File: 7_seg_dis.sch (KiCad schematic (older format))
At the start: 30 parts, among them U10 HDSP-7401, U5 74HC595, U6 74HC595, U7 74HC595, U8 HDSP-7401, U9 HDSP-7401

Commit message: reorganized schematic; added reverse polarity protection; start adding footprints
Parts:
- removed U10, U8, U9: HDSP-7401, Display_7Segment:HDSP-7401, symbol Display_Character:HDSP-7401
- added U? (x3): HDSP-7403, Display_7Segment:HDSP-7401, symbol Display_Character:HDSP-7403
- R10, R11, R12, R13, R14, R15, R16, R17, R18, R19, R20, R21, R22, R23, R24, R25, R26, R27, R4, R5, R6, R7, R8, R9: value R -> 330
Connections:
- net labels added: CLK, QH', RCLK, SER
- net labels removed: 7seg_POWER, SPI_1_CLK, SPI_1_CS, SPI_1_MOSI
- wire segments 174 -> 207
- no-connect marks 1 -> 0
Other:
- moved on the sheet: R10, R11, R12, R13, R14, R15, R16, R17, R18, R19, R20, R21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

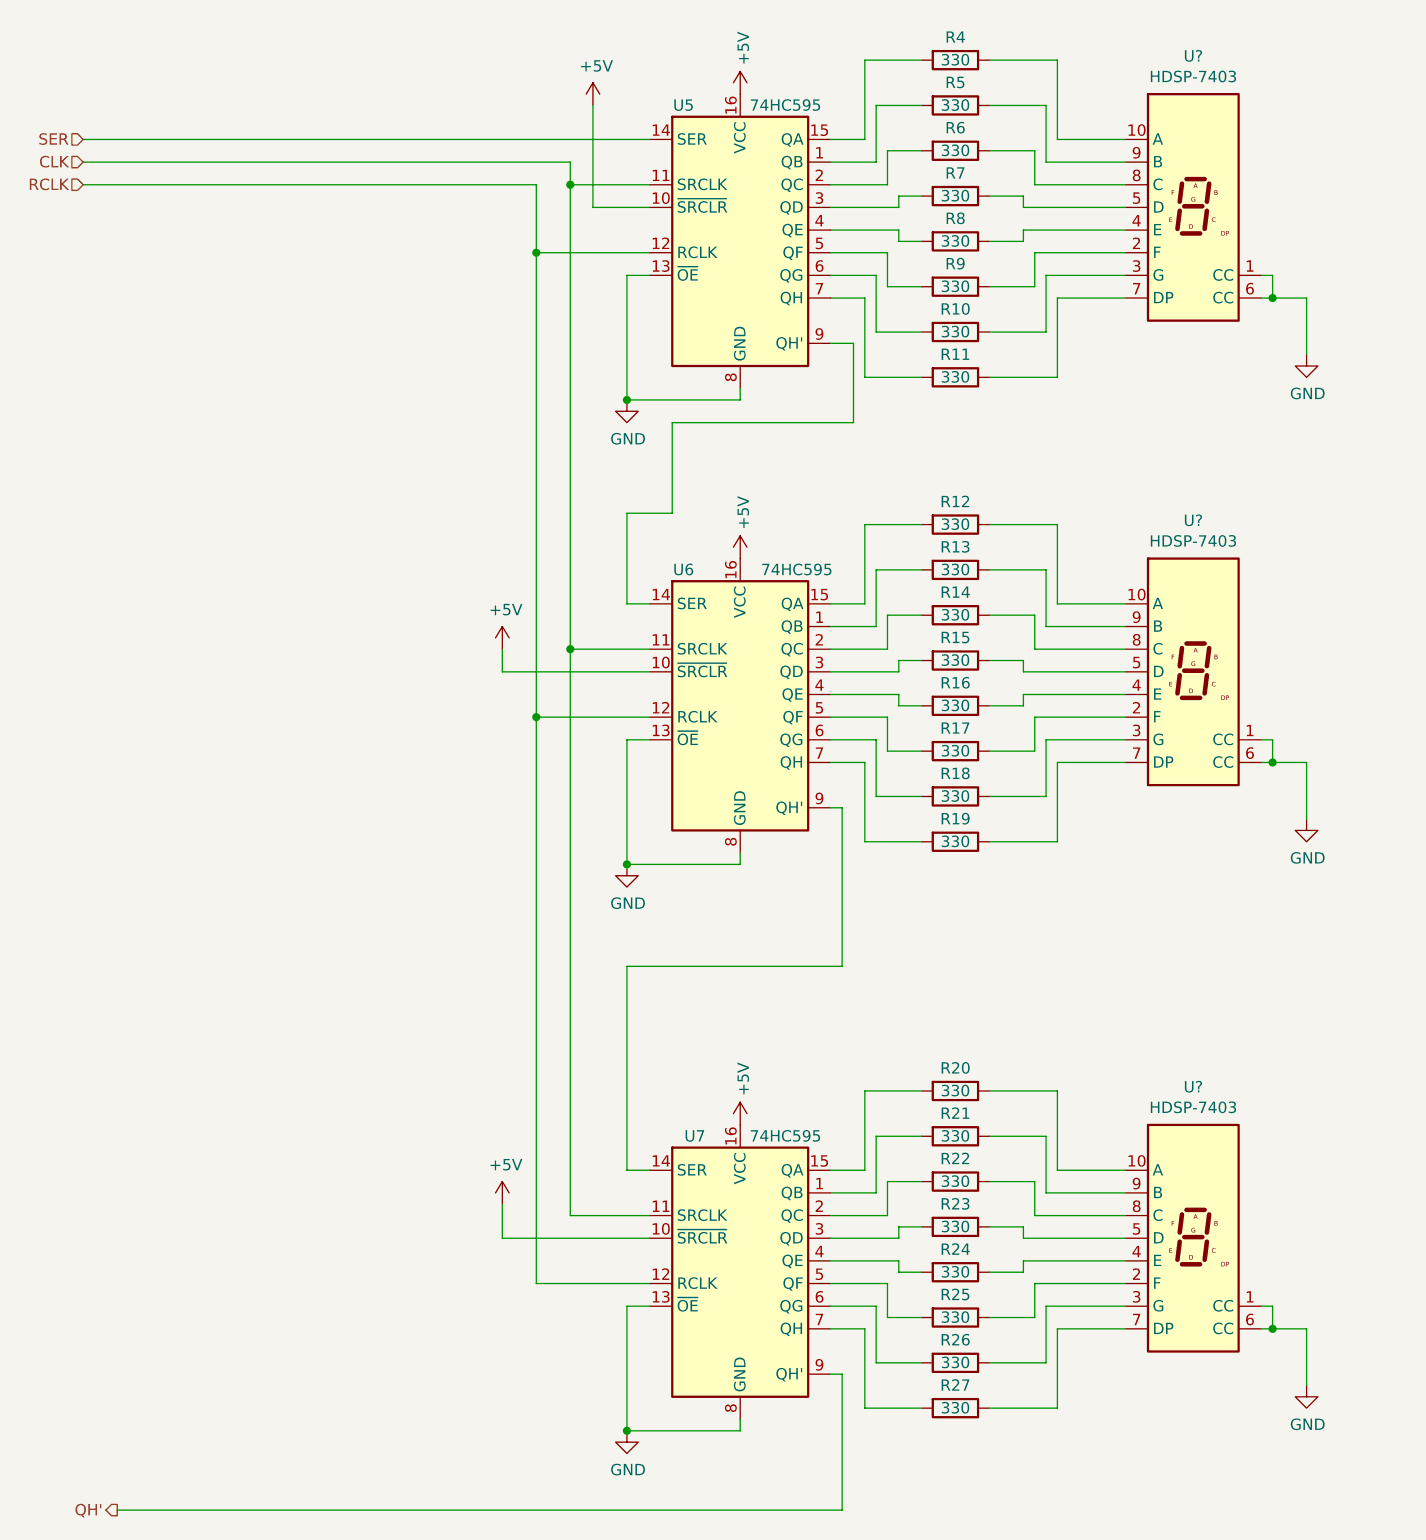
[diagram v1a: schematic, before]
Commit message: footprints; library for 7seg; start pcb layout
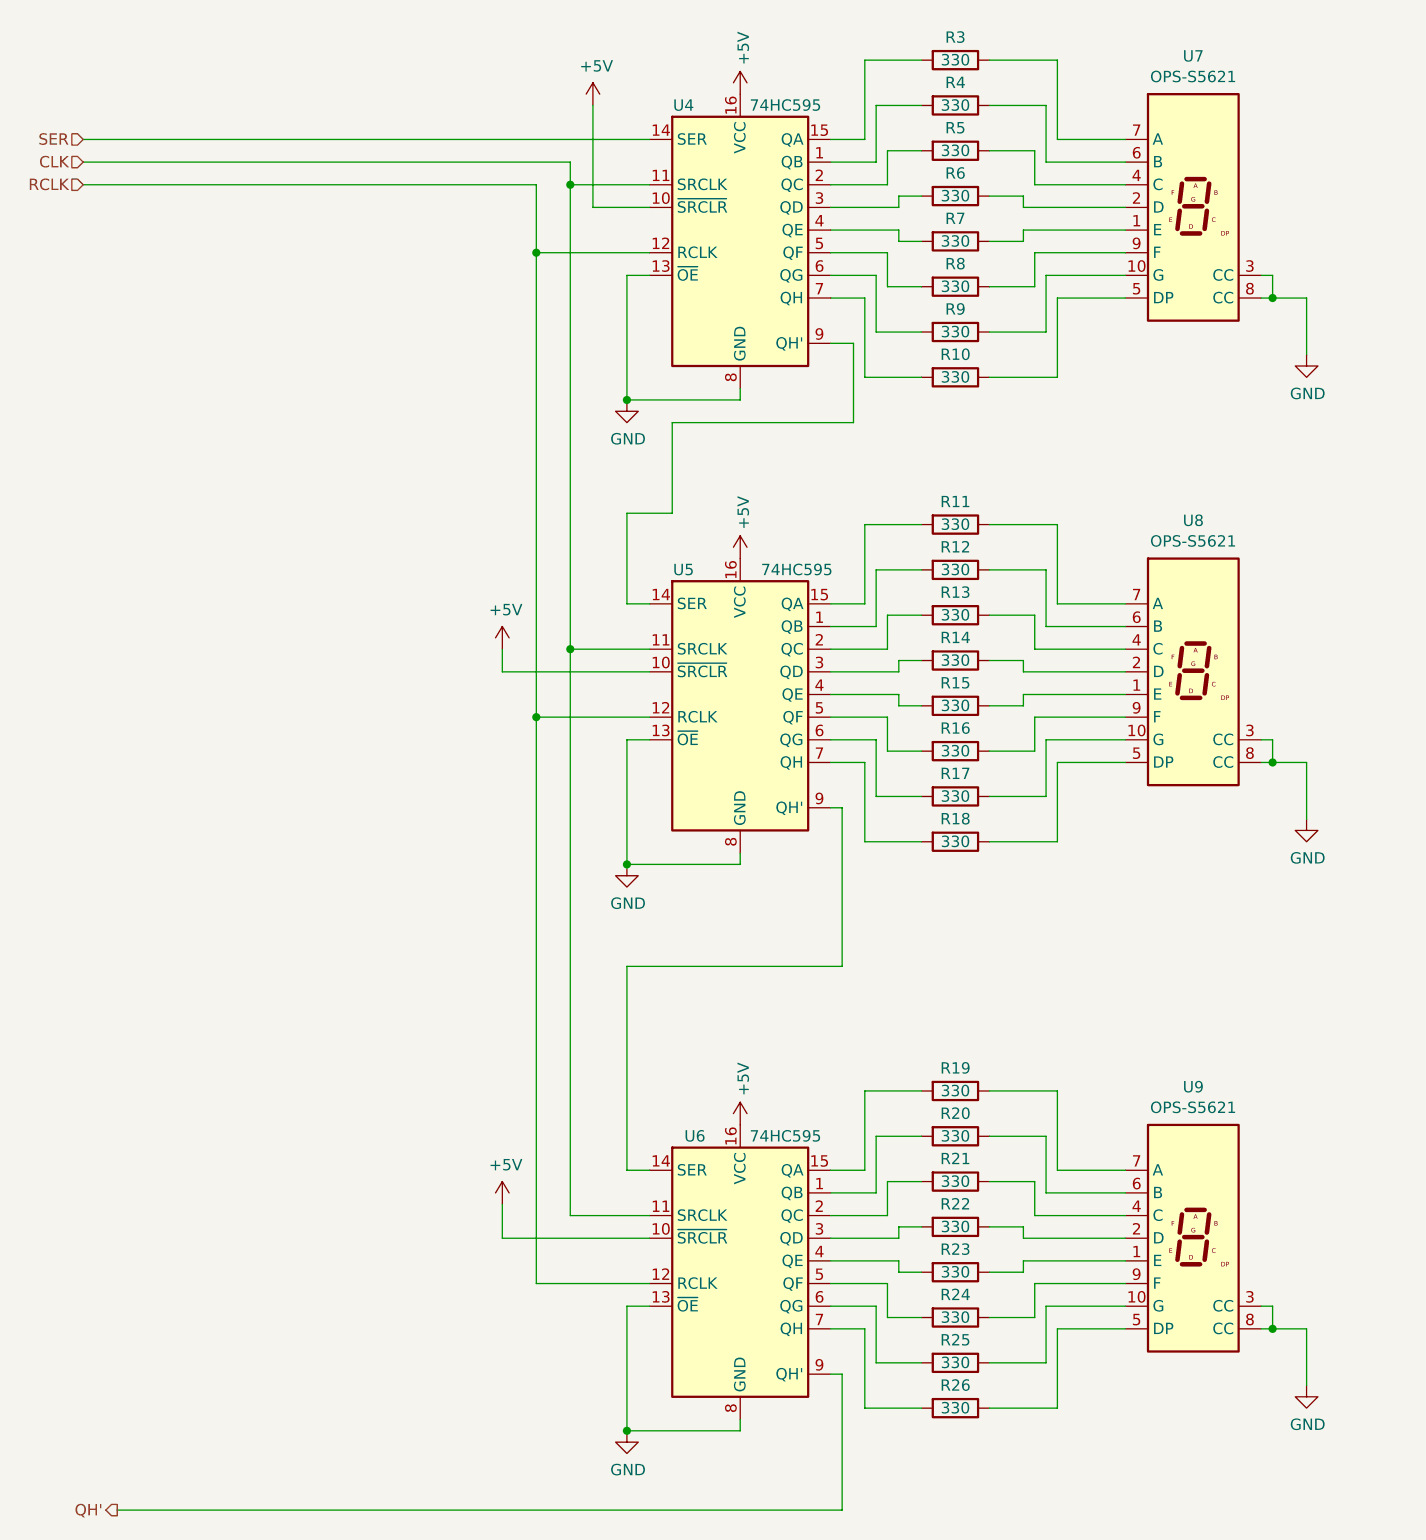
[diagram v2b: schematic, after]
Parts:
- removed U? (x3): HDSP-7403, Display_7Segment:HDSP-7401, symbol Display_Character:HDSP-7403
- added U7, U8, U9: OPS-S5621, PUTM_EV_Dashboard_2021:OPS-S5621LB-GW, symbol PUTM_EV_Dashboard_2021:OPS-S5621
- R10: renamed from R11; footprint (none) -> Resistor_SMD:R_0603_1608Metric
- R11: renamed from R12; footprint (none) -> Resistor_SMD:R_0603_1608Metric
- R12: renamed from R13; footprint (none) -> Resistor_SMD:R_0603_1608Metric
- R13: renamed from R14; footprint (none) -> Resistor_SMD:R_0603_1608Metric
- R14: renamed from R15; footprint (none) -> Resistor_SMD:R_0603_1608Metric
- R15: renamed from R16; footprint (none) -> Resistor_SMD:R_0603_1608Metric
- R16: renamed from R17; footprint (none) -> Resistor_SMD:R_0603_1608Metric
- R17: renamed from R18; footprint (none) -> Resistor_SMD:R_0603_1608Metric
- R18: renamed from R19; footprint (none) -> Resistor_SMD:R_0603_1608Metric
- R19: renamed from R20; footprint (none) -> Resistor_SMD:R_0603_1608Metric
- R20: renamed from R21; footprint (none) -> Resistor_SMD:R_0603_1608Metric
- R21: renamed from R22; footprint (none) -> Resistor_SMD:R_0603_1608Metric
- R22: renamed from R23; footprint (none) -> Resistor_SMD:R_0603_1608Metric
- R23: renamed from R24; footprint (none) -> Resistor_SMD:R_0603_1608Metric
- R24: renamed from R25; footprint (none) -> Resistor_SMD:R_0603_1608Metric
- R25: renamed from R26; footprint (none) -> Resistor_SMD:R_0603_1608Metric
- R26: renamed from R27; footprint (none) -> Resistor_SMD:R_0603_1608Metric
- R3: renamed from R4; footprint (none) -> Resistor_SMD:R_0603_1608Metric
- R4: renamed from R5; footprint (none) -> Resistor_SMD:R_0603_1608Metric
- R5: renamed from R6; footprint (none) -> Resistor_SMD:R_0603_1608Metric
- R6: renamed from R7; footprint (none) -> Resistor_SMD:R_0603_1608Metric
- R7: renamed from R8; footprint (none) -> Resistor_SMD:R_0603_1608Metric
- R8: renamed from R9; footprint (none) -> Resistor_SMD:R_0603_1608Metric
- R9: renamed from R10; footprint (none) -> Resistor_SMD:R_0603_1608Metric
- U4: renamed from U5; footprint (none) -> Package_SO:SOIC-16_3.9x9.9mm_P1.27mm
- U5: renamed from U6; footprint (none) -> Package_SO:SOIC-16_3.9x9.9mm_P1.27mm
- U6: renamed from U7; footprint (none) -> Package_SO:SOIC-16_3.9x9.9mm_P1.27mm
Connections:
- net GND: now also U7.3 (CC), U7.8 (CC), U8.3 (CC), U8.8 (CC), U9.3 (CC), U9.8 (CC)
- net at R3.1: now also U7.7 (A)
- net at R4.1: now also U7.6 (B)
- net at R5.1: now also U7.4 (C)
- net at R6.1: now also U7.2 (D)
- net at R7.1: now also U7.1 (E)
- net at R8.1: now also U7.9 (F)
- net at R9.1: now also U7.10 (G)
- net at R10.1: now also U7.5 (DP)
- net at R11.1: now also U8.7 (A)
- net at R12.1: now also U8.6 (B)
- net at R13.1: now also U8.4 (C)
- net at R14.1: now also U8.2 (D)
- net at R15.1: now also U8.1 (E)
- net at R16.1: now also U8.9 (F)
- net at R17.1: now also U8.10 (G)
- net at R18.1: now also U8.5 (DP)
- net at R19.1: now also U9.7 (A)
- net at R20.1: now also U9.6 (B)
- net at R21.1: now also U9.4 (C)
- net at R22.1: now also U9.2 (D)
- net at R23.1: now also U9.1 (E)
- net at R24.1: now also U9.9 (F)
- net at R25.1: now also U9.10 (G)
- net at R26.1: now also U9.5 (DP)

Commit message: Hardware update Approved
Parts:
- U7, U8, U9: footprint PUTM_EV_Dashboard_2021:OPS-S5621LB-GW -> PUTMotorsport_footprints:0.56” Case Mold Type LED Display
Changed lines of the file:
@@
 EESchema Schematic File Version 4
+LIBS:dash_hw-cache
 EELAYER 30 0
 EELAYER END
@@
 F 0 "U7" H 6000 2367 50  0000 C CNN
 F 1 "OPS-S5621" H 6000 2276 50  0000 C CNN
-F 2 "PUTM_EV_Dashboard_2021:OPS-S5621LB-GW" H 6000 1150 50  0001 C CNN
+F 2 "PUTMotorsport_footprints:0.56” Case Mold Type LED Display" H 6000 1150 50  0001 C CNN
 F 3 "https://docs.broadcom.com/docs/AV02-2553EN" H 6000 1700 50  0001 C CNN
 	1    6000 1700
@@
 F 0 "U8" H 6000 4417 50  0000 C CNN
 F 1 "OPS-S5621" H 6000 4326 50  0000 C CNN
-F 2 "PUTM_EV_Dashboard_2021:OPS-S5621LB-GW" H 6000 3200 50  0001 C CNN
+F 2 "PUTMotorsport_footprints:0.56” Case Mold Type LED Display" H 6000 3200 50  0001 C CNN
 F 3 "https://docs.broadcom.com/docs/AV02-2553EN" H 6000 3750 50  0001 C CNN
 	1    6000 3750
@@
 F 0 "U9" H 6000 6917 50  0000 C CNN
 F 1 "OPS-S5621" H 6000 6826 50  0000 C CNN
-F 2 "PUTM_EV_Dashboard_2021:OPS-S5621LB-GW" H 6000 5700 50  0001 C CNN
+F 2 "PUTMotorsport_footprints:0.56” Case Mold Type LED Display" H 6000 5700 50  0001 C CNN
 F 3 "https://docs.broadcom.com/docs/AV02-2553EN" H 6000 6250 50  0001 C CNN
 	1    6000 6250
